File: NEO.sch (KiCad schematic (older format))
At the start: 1 part

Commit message: NEO_modifiziert
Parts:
- removed U?: U-BLOX_NEO-M8P, symbol U-BLOX_NEO-M8P
- added C?: C, symbol C
- added L?: L, symbol L
- added R? (x4): R, symbol R
- added U?: U-BLOX_NEO-M8P, symbol U-BLOX_NEO-M8P
- added X?: ANT, symbol ANT
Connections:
- net labels added: +3V3, EXTINTO, GND, RESET_N, RX, SAFEBOOT_N, TX, USB_DM, USB_DP
- wire segments 0 -> 30
- no-connect marks 0 -> 4
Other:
- note added: "C94-M8P - User Guide \n9 Schematic \n\n"
- note added: "NEO-M8P - Hardware Integration Manual \nA.1 Recommended parts \nRecommended antennas \n"
- note added: "NEO-M8P - Hardware Integration Manual \nActive antenna design using VCC_RF pin to supply the active antenna"

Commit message: NEO N8P durch M8N ersätzt
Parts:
- removed R?: R, symbol R
- removed U?: U-BLOX_NEO-M8P, symbol U-BLOX_NEO-M8P
- added R?: 10k, Passives:R0402N, symbol R
- added U?: U-BLOX-NEO-M8N, symbol U-BLOX-NEO-M8N
- C?: value C -> 10n, 16V; footprint (none) -> Passives:C0402N
- L?: value L -> 27n; footprint (none) -> Passives:L0402N
- R?: value R -> 10 Ω ± 10%, min 0.250 W; footprint (none) -> Passives:R0402N
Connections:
- net labels added: ~RESET
- net labels removed: EXTINTO, RESET_N, SAFEBOOT_N
- wire segments 30 -> 31
- no-connect marks 4 -> 9
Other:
- note added: ""high" = Turn OFF antenna supply\n"low" = Turn ON antenna supply \n"
- note added: "Brücke?"
- note added: "Configurable Timepulse signal LED dran?"
- note added: "EXTINT: External interrupt\n"
- note added: "If no backup supply voltage is available, \nconnect the V_BCKP pin to VCC."
- note added: "If open, UART and DDC are available."
- note added: "If the USB interface is not used, the VDD_USB \npin must be connected to GND"
- note added: "VCC_RF can be used to power \nan external active antenna."
- moved on the sheet: C?, L?, R?, X?

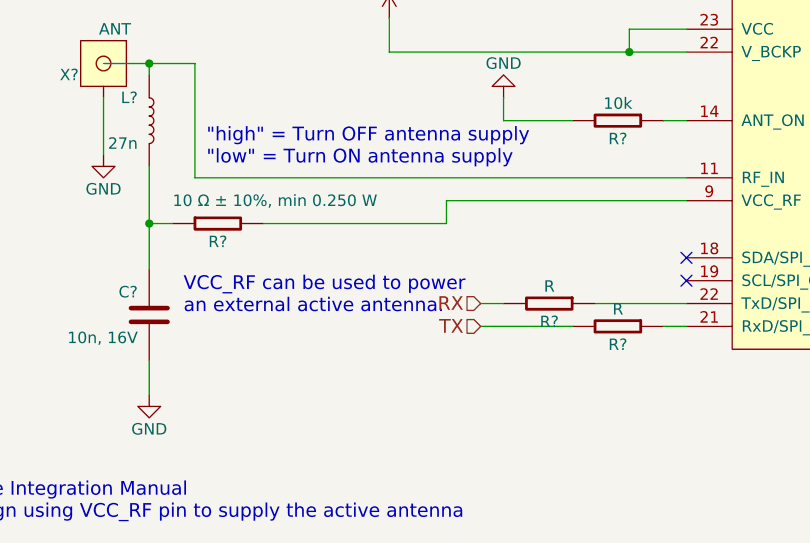
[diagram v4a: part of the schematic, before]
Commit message: footprints ergänzt
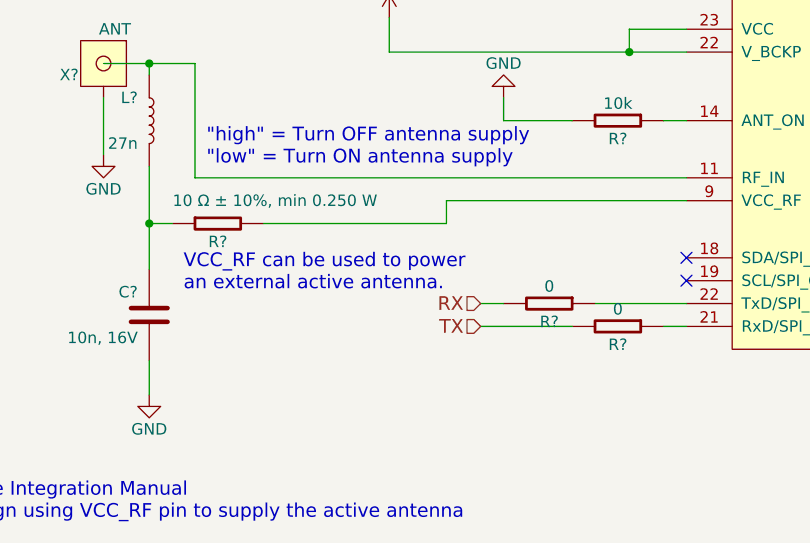
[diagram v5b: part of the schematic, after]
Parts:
- removed R?: R, symbol R
- added R?: 0, Passives:R0402N, symbol R
- R?: value R -> 0; footprint (none) -> Passives:R0402N
- U?: footprint (none) -> Communication:UBLOX_NEO-M8P
- X?: footprint (none) -> Connector:U.FL-R-SMT
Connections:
- net TX: now also R?.2
- net at U?.21 (RxD/SPI_MOSI): now also R?.1
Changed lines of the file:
@@
-$Comp
-L R R?
-U 1 1 57191463
-P 4950 4300
-F 0 "R?" V 5030 4300 50  0000 C CNN
-F 1 "R" V 4875 4300 50  0000 C CNN
-F 2 "" V 4880 4300 30  0000 C CNN
-F 3 "" H 4950 4300 30  0000 C CNN
-	1    4950 4300
-	0    1    1    0
-$EndComp
 $Comp
 L R R?
@@
 P 4650 4200
 F 0 "R?" V 4730 4200 50  0000 C CNN
-F 1 "R" V 4575 4200 50  0000 C CNN
-F 2 "" V 4580 4200 30  0000 C CNN
+F 1 "0" V 4575 4200 50  0000 C CNN
+F 2 "Passives:R0402N" V 4580 4200 30  0001 C CNN
 F 3 "" H 4650 4200 30  0000 C CNN
 	1    4650 4200
@@
 F 0 "X?" H 2850 3100 50  0000 C CNN
 F 1 "ANT" H 2650 3300 50  0000 C CNN
-F 2 "" H 2700 3150 60  0000 C CNN
+F 2 "Connector:U.FL-R-SMT" H 2700 3150 60  0001 C CNN
 F 3 "" H 2700 3150 60  0000 C CNN
 	1    2700 3150
@@
 F 0 "U?" H 6900 2500 60  0000 C CNN
 F 1 "U-BLOX-NEO-M8N" H 5900 4750 60  0000 C CNN
-F 2 "" H 6200 4100 60  0000 C CNN
+F 2 "Communication:UBLOX_NEO-M8P" H 6200 4100 60  0001 C CNN
 F 3 "" H 6200 4100 60  0000 C CNN
 	1    6200 3500
@@
 Text Notes 3500 2400 0    60   ~ 0
 If open, UART and DDC are available.
-Text Notes 3050 4250 0    60   ~ 0
+Text Notes 3050 4150 0    60   ~ 0
 VCC_RF can be used to power \nan external active antenna.
 Wire Wire Line
@@
 Wire Wire Line
 	4450 3400 4750 3400
+$Comp
+L R R?
+U 1 1 5723EA45
+P 4950 4300
+F 0 "R?" V 5030 4300 50  0000 C CNN
+F 1 "0" V 4875 4300 50  0000 C CNN
+F 2 "Passives:R0402N" V 4880 4300 30  0001 C CNN
+F 3 "" H 4950 4300 30  0000 C CNN
+	1    4950 4300
+	0    1    1    0
+$EndComp
 $EndSCHEMATC

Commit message: added some footprints
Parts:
- added C601, C602: 100n, Passives:C0402N, symbol C
- gave numbers to parts that had none: 8
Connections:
- net +3V3: now also C601.1, C602.1
- net GND: now also C601.2, C602.2
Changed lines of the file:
@@
 	3950 3100 3950 2950
 $Comp
-L +3V3 #PWR?
+L +3V3 #PWR0135
 U 1 1 57190E14
 P 3950 2950
-F 0 "#PWR?" H 3950 2800 50  0001 C CNN
+F 0 "#PWR0135" H 3950 2800 50  0001 C CNN
 F 1 "+3V3" H 3950 3090 50  0000 C CNN
 F 2 "" H 3950 2950 50  0000 C CNN
@@
 $EndComp
 $Comp
-L GND #PWR?
+L GND #PWR0136
 U 1 1 57190E68
 P 7400 2900
-F 0 "#PWR?" H 7400 2650 50  0001 C CNN
+F 0 "#PWR0136" H 7400 2650 50  0001 C CNN
 F 1 "GND" H 7400 2750 50  0000 C CNN
 F 2 "" H 7400 2900 50  0000 C CNN
@@
 USB_DM
 $Comp
-L R R?
+L R R602
 U 1 1 57191481
 P 4650 4200
-F 0 "R?" V 4730 4200 50  0000 C CNN
+F 0 "R602" V 4730 4200 50  0000 C CNN
 F 1 "0" V 4575 4200 50  0000 C CNN
 F 2 "Passives:R0402N" V 4580 4200 30  0001 C CNN
@@
 TX
 $Comp
-L ANT X?
+L ANT X601
 U 1 1 5719155A
 P 2700 3150
-F 0 "X?" H 2850 3100 50  0000 C CNN
+F 0 "X601" H 2850 3100 50  0000 C CNN
 F 1 "ANT" H 2650 3300 50  0000 C CNN
 F 2 "Connector:U.FL-R-SMT" H 2700 3150 60  0001 C CNN
@@
 $EndComp
 $Comp
-L L L?
+L L L601
 U 1 1 571915BF
 P 2900 3400
-F 0 "L?" H 2950 3500 50  0000 L CNN
+F 0 "L601" H 2950 3500 50  0000 L CNN
 F 1 "27n" H 2950 3300 50  0000 L CNN
 F 2 "Passives:L0402N" H 2938 3250 30  0001 C CNN
@@
 	3100 3150 2700 3150
 $Comp
-L R R?
+L R R601
 U 1 1 57191704
 P 3200 3850
-F 0 "R?" V 3280 3850 50  0000 C CNN
+F 0 "R601" V 3280 3850 50  0000 C CNN
 F 1 "10 Ω ± 10%, min 0.250 W" V 3100 3600 50  0000 C CNN
 F 2 "Passives:R0402N" V 3130 3850 30  0001 C CNN
@@
 $EndComp
 $Comp
-L C C?
+L C C603
 U 1 1 57191740
 P 2900 4250
-F 0 "C?" H 2950 4350 50  0000 L CNN
+F 0 "C603" H 2950 4350 50  0000 L CNN
 F 1 "10n, 16V" H 2950 4150 50  0000 L CNN
 F 2 "Passives:C0402N" H 2938 4100 30  0001 C CNN
@@
 Connection ~ 2900 3850
 $Comp
-L GND #PWR?
+L GND #PWR0137
 U 1 1 57191865
 P 2900 4600
-F 0 "#PWR?" H 2900 4350 50  0001 C CNN
+F 0 "#PWR0137" H 2900 4350 50  0001 C CNN
 F 1 "GND" H 2900 4450 50  0000 C CNN
 F 2 "" H 2900 4600 50  0000 C CNN
@@
 $EndComp
 $Comp
-L GND #PWR?
+L GND #PWR0138
 U 1 1 57191891
 P 2700 3550
-F 0 "#PWR?" H 2700 3300 50  0001 C CNN
+F 0 "#PWR0138" H 2700 3300 50  0001 C CNN
 F 1 "GND" H 2700 3400 50  0000 C CNN
 F 2 "" H 2700 3550 50  0000 C CNN
@@
 NEO-M8P - Hardware Integration Manual \nActive antenna design using VCC_RF pin to supply the active antenna
 $Comp
-L U-BLOX-NEO-M8N U?
+L U-BLOX-NEO-M8N U601
 U 1 1 57210515
 P 6200 3500
-F 0 "U?" H 6900 2500 60  0000 C CNN
+F 0 "U601" H 6900 2500 60  0000 C CNN
 F 1 "U-BLOX-NEO-M8N" H 5900 4750 60  0000 C CNN
 F 2 "Communication:UBLOX_NEO-M8P" H 6200 4100 60  0001 C CNN
@@
 If the USB interface is not used, the VDD_USB \npin must be connected to GND
 $Comp
-L GND #PWR?
+L GND #PWR0139
 U 1 1 57211386
 P 7400 3900
-F 0 "#PWR?" H 7400 3650 50  0001 C CNN
+F 0 "#PWR0139" H 7400 3650 50  0001 C CNN
 F 1 "GND" H 7400 3750 50  0000 C CNN
 F 2 "" H 7400 3900 50  0000 C CNN
@@
 "high" = Turn OFF antenna supply\n"low" = Turn ON antenna supply \n
 $Comp
-L R R?
+L R R603
 U 1 1 572118C1
 P 4950 3400
-F 0 "R?" V 5030 3400 50  0000 C CNN
+F 0 "R603" V 5030 3400 50  0000 C CNN
 F 1 "10k" V 4875 3400 50  0000 C CNN
 F 2 "Passives:R0402N" V 4880 3400 30  0001 C CNN
@@
 $EndComp
 $Comp
-L GND #PWR?
+L GND #PWR0140
 U 1 1 57211964
 P 4450 3300
-F 0 "#PWR?" H 4450 3050 50  0001 C CNN
+F 0 "#PWR0140" H 4450 3050 50  0001 C CNN
 F 1 "GND" H 4450 3150 50  0000 C CNN
 F 2 "" H 4450 3300 50  0000 C CNN
@@
 	4450 3400 4750 3400
 $Comp
-L R R?
+L R R604
 U 1 1 5723EA45
 P 4950 4300
-F 0 "R?" V 5030 4300 50  0000 C CNN
+F 0 "R604" V 5030 4300 50  0000 C CNN
 F 1 "0" V 4875 4300 50  0000 C CNN
 F 2 "Passives:R0402N" V 4880 4300 30  0001 C CNN
@@
 	0    1    1    0
 $EndComp
+$Comp
+L C C601
+U 1 1 57260AE1
+P 1200 3400
+F 0 "C601" H 1250 3500 50  0000 L CNN
+F 1 "100n" H 1250 3300 50  0000 L CNN
+F 2 "Passives:C0402N" H 1238 3250 30  0001 C CNN
+F 3 "" H 1250 3500 60  0000 C CNN
+	1    1200 3400
+	1    0    0    -1
+$EndComp
+$Comp
+L C C602
+U 1 1 57260BB7
+P 1550 3400
+F 0 "C602" H 1600 3500 50  0000 L CNN
+F 1 "100n" H 1600 3300 50  0000 L CNN
+F 2 "Passives:C0402N" H 1588 3250 30  0001 C CNN
+F 3 "" H 1600 3500 60  0000 C CNN
+	1    1550 3400
+	1    0    0    -1
+$EndComp
+$Comp
+L +3V3 #PWR0141
+U 1 1 57260BFE
+P 1200 3000
+F 0 "#PWR0141" H 1200 2850 50  0001 C CNN
+F 1 "+3V3" H 1200 3140 50  0000 C CNN
+F 2 "" H 1200 3000 50  0000 C CNN
+F 3 "" H 1200 3000 50  0000 C CNN
+	1    1200 3000
+	1    0    0    -1
+$EndComp
+$Comp
+L GND #PWR0142
+U 1 1 57260C27
+P 1200 3800
+F 0 "#PWR0142" H 1200 3550 50  0001 C CNN
+F 1 "GND" H 1200 3650 50  0000 C CNN
+F 2 "" H 1200 3800 50  0000 C CNN
+F 3 "" H 1200 3800 50  0000 C CNN
+	1    1200 3800
+	-1   0    0    -1
+$EndComp
+Wire Wire Line
+	1200 3000 1200 3200
+Wire Wire Line
+	1200 3050 1550 3050
+Wire Wire Line
+	1550 3050 1550 3200
+Connection ~ 1200 3050
+Wire Wire Line
+	1200 3600 1200 3800
+Wire Wire Line
+	1200 3700 1550 3700
+Wire Wire Line
+	1550 3700 1550 3600
+Connection ~ 1200 3700
 $EndSCHEMATC

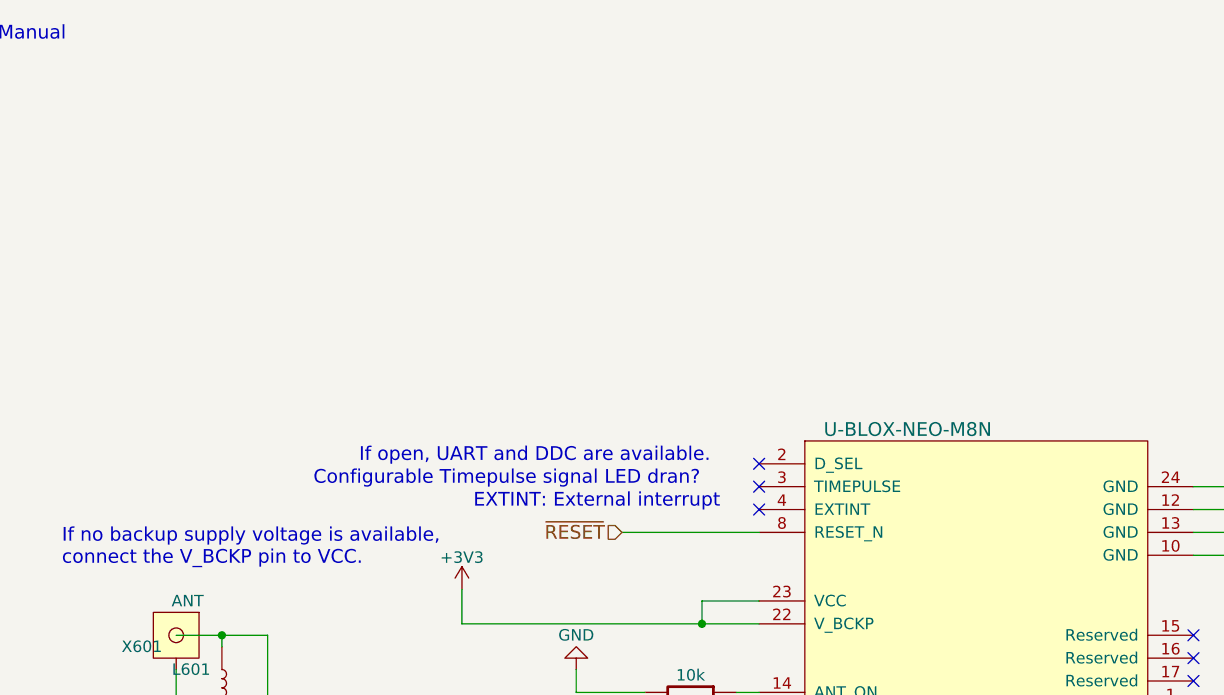
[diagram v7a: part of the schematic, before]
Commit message: adjusted power supply and sensors
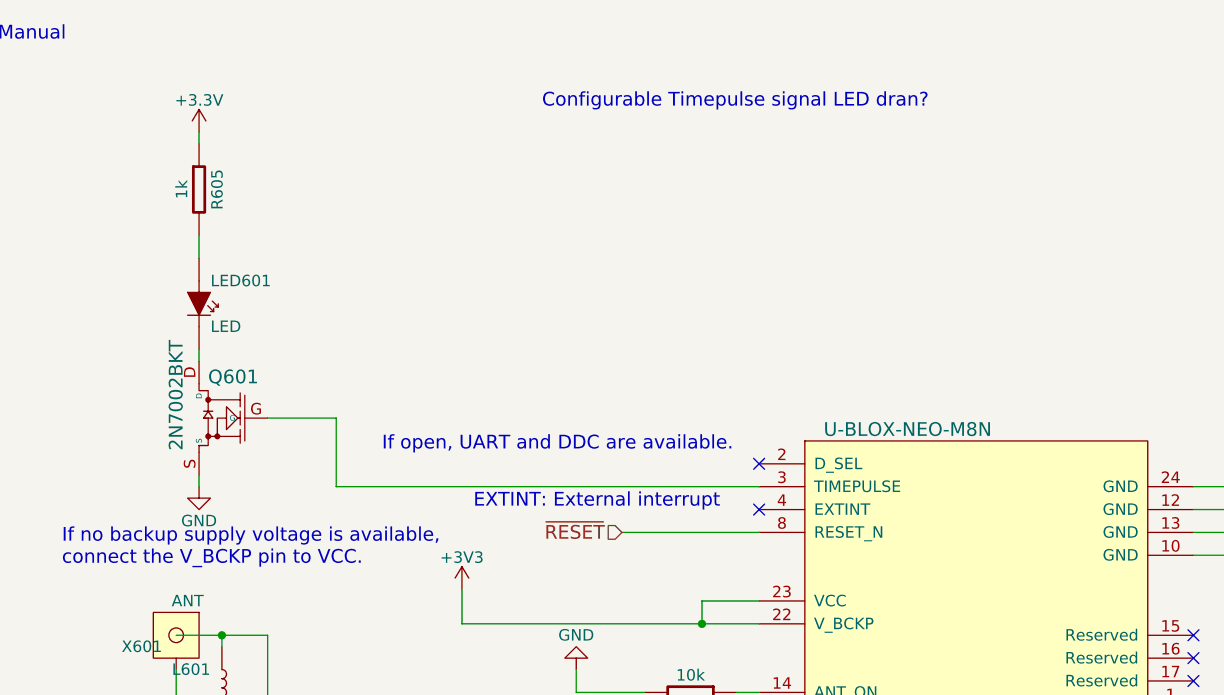
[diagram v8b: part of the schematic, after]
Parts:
- added LED601: LED, symbol LED
- added Q601: 2N7002BKT, symbol NMOS
- added R605: 1k, Passives:R0402N, symbol R
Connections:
- net +3V3: now also R605.1
- net GND: now also Q601.S
- net at U601.3 (TIMEPULSE): now also Q601.G
- new net: LED601.A, R605.2
- new net: LED601.C, Q601.D
- no-connect marks 9 -> 8
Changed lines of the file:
@@
 	3950 3100 3950 2950
 $Comp
-L +3V3 #PWR605
+L +3V3 #PWR607
 U 1 1 57190E14
 P 3950 2950
-F 0 "#PWR605" H 3950 2800 50  0001 C CNN
+F 0 "#PWR607" H 3950 2800 50  0001 C CNN
 F 1 "+3V3" H 3950 3090 50  0000 C CNN
 F 2 "" H 3950 2950 50  0000 C CNN
@@
 $EndComp
 $Comp
-L GND #PWR607
+L GND #PWR609
 U 1 1 57190E68
 P 7400 2900
-F 0 "#PWR607" H 7400 2650 50  0001 C CNN
+F 0 "#PWR609" H 7400 2650 50  0001 C CNN
 F 1 "GND" H 7400 2750 50  0000 C CNN
 F 2 "" H 7400 2900 50  0000 C CNN
@@
 Connection ~ 2900 3850
 $Comp
-L GND #PWR604
+L GND #PWR606
 U 1 1 57191865
 P 2900 4600
-F 0 "#PWR604" H 2900 4350 50  0001 C CNN
+F 0 "#PWR606" H 2900 4350 50  0001 C CNN
 F 1 "GND" H 2900 4450 50  0000 C CNN
 F 2 "" H 2900 4600 50  0000 C CNN
@@
 Text Notes 1400 5150 0    60   ~ 0
 NEO-M8P - Hardware Integration Manual \nActive antenna design using VCC_RF pin to supply the active antenna
-$Comp
-L U-BLOX-NEO-M8N U601
-U 1 1 57210515
-P 6200 3500
-F 0 "U601" H 6900 2500 60  0000 C CNN
-F 1 "U-BLOX-NEO-M8N" H 5900 4750 60  0000 C CNN
-F 2 "Communication:UBLOX_NEO-M8P" H 6200 4100 60  0001 C CNN
-F 3 "" H 6200 4100 60  0000 C CNN
-	1    6200 3500
-	1    0    0    -1
-$EndComp
 Wire Wire Line
 	7150 2500 7400 2500
@@
 EXTINT: External interrupt\n
 NoConn ~ 5250 2600
-Text Notes 3500 2400 0    60   ~ 0
+Text Notes 3600 2350 0    60   ~ 0
 If open, UART and DDC are available.
 Text Notes 3050 4150 0    60   ~ 0
@@
 NoConn ~ 5250 4000
 NoConn ~ 5250 4100
-NoConn ~ 5250 2500
-Text Notes 3300 2500 0    60   ~ 0
+Text Notes 4300 850  0    60   ~ 0
 Configurable Timepulse signal LED dran?
 Text Notes 2200 2850 0    60   ~ 0
@@
 If the USB interface is not used, the VDD_USB \npin must be connected to GND
 $Comp
-L GND #PWR608
+L GND #PWR610
 U 1 1 57211386
 P 7400 3900
-F 0 "#PWR608" H 7400 3650 50  0001 C CNN
+F 0 "#PWR610" H 7400 3650 50  0001 C CNN
 F 1 "GND" H 7400 3750 50  0000 C CNN
 F 2 "" H 7400 3900 50  0000 C CNN
@@
 $EndComp
 $Comp
-L GND #PWR606
+L GND #PWR608
 U 1 1 57211964
 P 4450 3300
-F 0 "#PWR606" H 4450 3050 50  0001 C CNN
+F 0 "#PWR608" H 4450 3050 50  0001 C CNN
 F 1 "GND" H 4450 3150 50  0000 C CNN
 F 2 "" H 4450 3300 50  0000 C CNN
@@
 	1550 3700 1550 3600
 Connection ~ 1200 3700
+$Comp
+L LED LED601
+U 1 1 572B1808
+P 2800 1700
+F 0 "LED601" H 2850 1800 50  0000 L CNN
+F 1 "LED" H 2850 1600 50  0000 L CNN
+F 2 "" H 2838 1550 30  0001 C CNN
+F 3 "" H 2800 1700 60  0000 C CNN
+	1    2800 1700
+	1    0    0    -1
+$EndComp
+$Comp
+L R R605
+U 1 1 572B1841
+P 2800 1200
+F 0 "R605" V 2880 1200 50  0000 C CNN
+F 1 "1k" V 2725 1200 50  0000 C CNN
+F 2 "Passives:R0402N" V 2730 1200 30  0001 C CNN
+F 3 "" H 2800 1200 30  0000 C CNN
+	1    2800 1200
+	1    0    0    -1
+$EndComp
+$Comp
+L U-BLOX-NEO-M8N U601
+U 1 1 57210515
+P 6200 3500
+F 0 "U601" H 6900 2500 60  0000 C CNN
+F 1 "U-BLOX-NEO-M8N" H 5900 4750 60  0000 C CNN
+F 2 "Communication:UBLOX_NEO-M8P" H 6200 4100 60  0001 C CNN
+F 3 "" H 6200 4100 60  0000 C CNN
+	1    6200 3500
+	1    0    0    -1
+$EndComp
+$Comp
+L NMOS Q601
+U 1 1 572B29ED
+P 2800 2200
+F 0 "Q601" H 2650 2380 60  0000 C CNN
+F 1 "2N7002BKT" V 2900 2300 60  0000 C CNN
+F 2 "" H 2150 2525 60  0001 C CNN
+F 3 "" H 2150 2525 60  0000 C CNN
+	1    2800 2200
+	-1   0    0    -1
+$EndComp
+$Comp
+L GND #PWR605
+U 1 1 572B35D6
+P 2800 2500
+F 0 "#PWR605" H 2800 2250 50  0001 C CNN
+F 1 "GND" H 2800 2350 50  0000 C CNN
+F 2 "" H 2800 2500 50  0000 C CNN
+F 3 "" H 2800 2500 50  0000 C CNN
+	1    2800 2500
+	1    0    0    -1
+$EndComp
+Wire Wire Line
+	2800 1900 2800 1950
+Wire Wire Line
+	2800 2450 2800 2500
+Wire Wire Line
+	2800 1400 2800 1500
+$Comp
+L +3.3V #PWR604
+U 1 1 572B3723
+P 2800 950
+F 0 "#PWR604" H 2800 800 50  0001 C CNN
+F 1 "+3.3V" H 2800 1090 50  0000 C CNN
+F 2 "" H 2800 950 50  0000 C CNN
+F 3 "" H 2800 950 50  0000 C CNN
+	1    2800 950
+	1    0    0    -1
+$EndComp
+Wire Wire Line
+	2800 950  2800 1000
+Wire Wire Line
+	3100 2200 3400 2200
+Wire Wire Line
+	3400 2200 3400 2500
+Wire Wire Line
+	3400 2500 5250 2500
 $EndSCHEMATC
